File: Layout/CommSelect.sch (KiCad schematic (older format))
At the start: 1 part

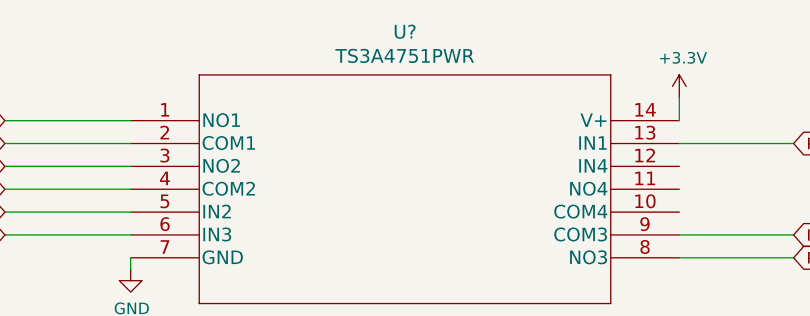
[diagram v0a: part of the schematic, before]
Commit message: Add more sheets. Add LEDs
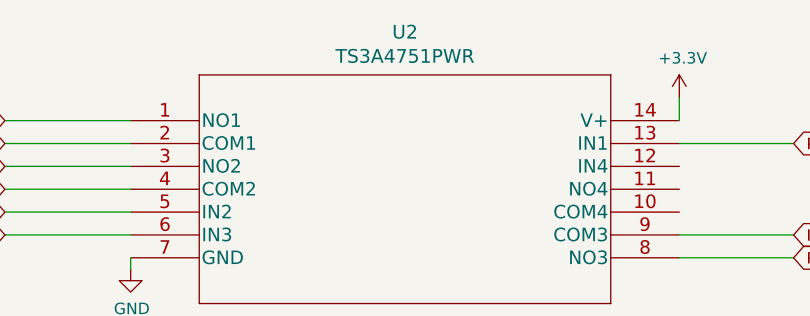
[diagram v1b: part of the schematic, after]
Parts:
- gave numbers to parts that had none: 1
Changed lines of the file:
@@
 $Descr A4 11693 8268
 encoding utf-8
-Sheet 4 4
+Sheet 4 7
 Title ""
 Date ""
@@
 U 1 1 5F378E97
 P 4350 3250
-F 0 "U?" H 5550 3637 60  0000 C CNN
+AR Path="/5F378E97" Ref="U?"  Part="1"
+AR Path="/5F373590/5F378E97" Ref="U2"  Part="1"
+F 0 "U2" H 5550 3637 60  0000 C CNN
 F 1 "TS3A4751PWR" H 5550 3531 60  0000 C CNN
 F 2 "PW14" H 5550 3490 60  0001 C CNN
@@
 U 1 1 5F378E9D
 P 6750 3150
-F 0 "#PWR?" H 6750 3000 50  0001 C CNN
+AR Path="/5F378E9D" Ref="#PWR?"  Part="1"
+AR Path="/5F373590/5F378E9D" Ref="#PWR0114"  Part="1"
+F 0 "#PWR0114" H 6750 3000 50  0001 C CNN
 F 1 "+3.3V" H 6765 3323 50  0000 C CNN
 F 2 "" H 6750 3150 50  0001 C CNN
@@
 U 1 1 5F378EA4
 P 4350 3900
-F 0 "#PWR?" H 4350 3650 50  0001 C CNN
+AR Path="/5F378EA4" Ref="#PWR?"  Part="1"
+AR Path="/5F373590/5F378EA4" Ref="#PWR0115"  Part="1"
+F 0 "#PWR0115" H 4350 3650 50  0001 C CNN
 F 1 "GND" H 4355 3727 50  0000 C CNN
 F 2 "" H 4350 3900 50  0001 C CNN

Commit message: Update footprints and references
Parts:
- U2: footprint PW14 -> Package_SO:TSSOP-14_4.4x5mm_P0.65mm
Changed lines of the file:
@@
 F 0 "U2" H 5550 3637 60  0000 C CNN
 F 1 "TS3A4751PWR" H 5550 3531 60  0000 C CNN
-F 2 "PW14" H 5550 3490 60  0001 C CNN
+F 2 "Package_SO:TSSOP-14_4.4x5mm_P0.65mm" H 5550 3490 60  0001 C CNN
 F 3 "" H 4350 3250 60  0000 C CNN
 	1    4350 3250

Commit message: Generate PCB layout
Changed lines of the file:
@@
 Text GLabel 7250 3850 2    50   Input ~ 0
 PORT3_IO
+Text GLabel 5050 4550 0    50   Input ~ 0
+TX
+Text GLabel 5050 4750 0    50   Input ~ 0
+RX
+Wire Wire Line
+	5050 4550 5150 4550
+Wire Wire Line
+	5150 4550 5150 4750
+Wire Wire Line
+	5150 4750 5050 4750
+Wire Wire Line
+	5150 4550 5850 4550
+Connection ~ 5150 4550
+Text GLabel 5850 4550 2    50   Input ~ 0
+IO_COM
 $EndSCHEMATC

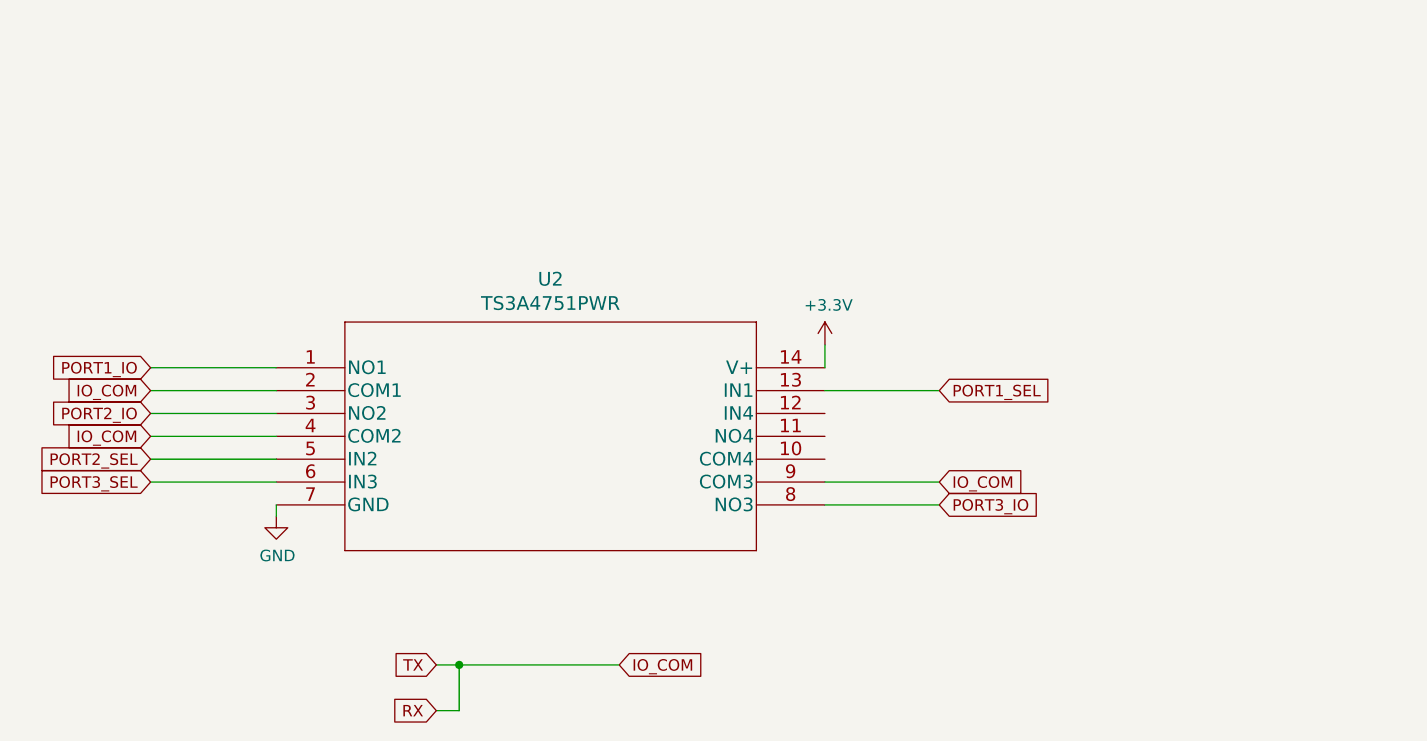
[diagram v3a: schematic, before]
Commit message: Update schematic for new processor
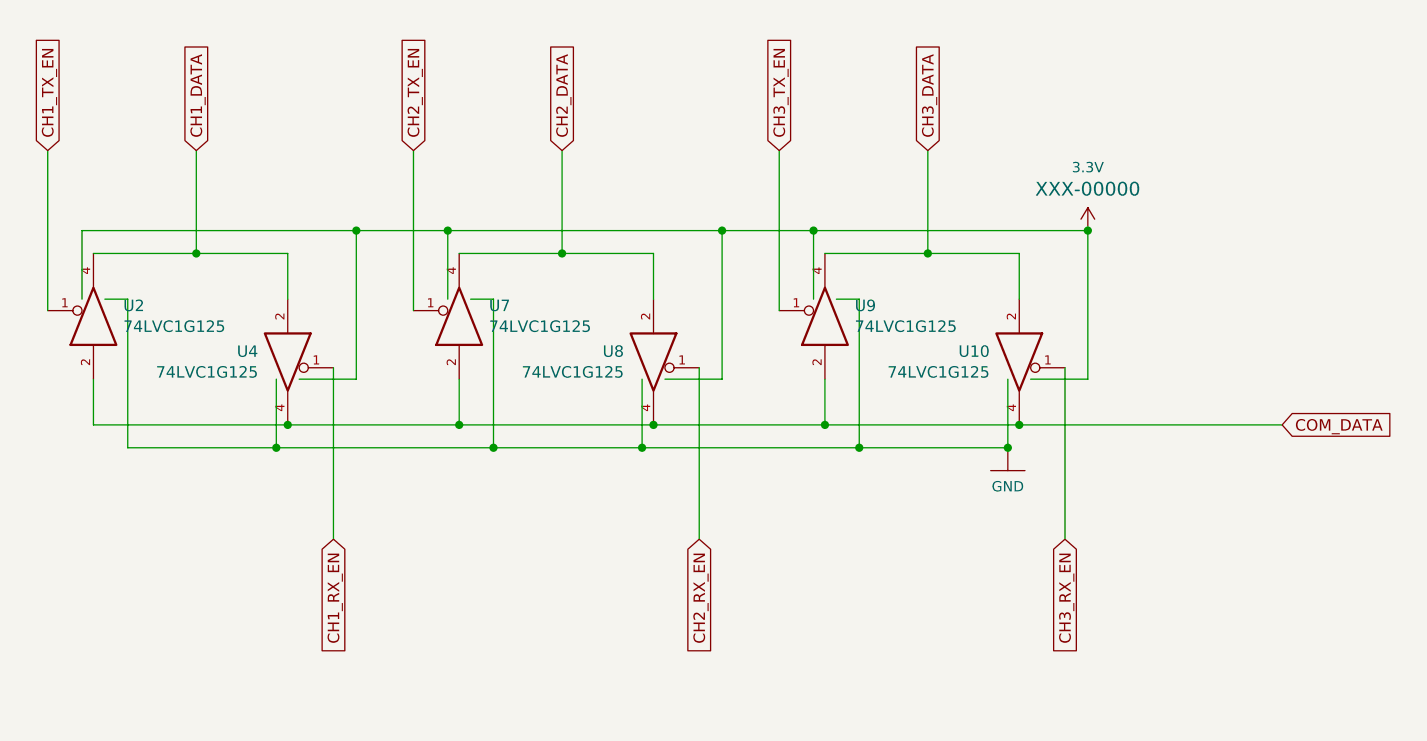
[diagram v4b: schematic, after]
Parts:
- removed U2: TS3A4751PWR, Package_SO:TSSOP-14_4.4x5mm_P0.65mm, symbol TS3A475:TS3A4751PWR
- added U10, U2, U4, U7, U8, U9: 74LVC1G125, Package_TO_SOT_SMD:SOT-353_SC-70-5_Handsoldering, symbol 74xGxx:74LVC1G125
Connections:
- net GND: now also U10.3 (GND), U2.3 (GND), U4.3 (GND), U7.3 (GND), U8.3 (GND), U9.3 (GND)
- new net 3.3V: U10.5 (VCC), U2.5 (VCC), U4.5 (VCC), U7.5 (VCC), U8.5 (VCC), U9.5 (VCC)
- new net CH1_DATA: U2.4, U4.2
- new net CH1_RX_EN: U4.1
- new net CH1_TX_EN: U2.1
- new net CH2_DATA: U7.4, U8.2
- new net CH2_RX_EN: U8.1
- new net CH2_TX_EN: U7.1
- new net CH3_DATA: U10.2, U9.4
- new net CH3_RX_EN: U10.1
- new net CH3_TX_EN: U9.1
- new net COM_DATA: U10.4, U2.2, U4.4, U7.2, U8.4, U9.2
